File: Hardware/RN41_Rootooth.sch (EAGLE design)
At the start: 23 parts, among them Q1 MOSFET-NCHANNELSMD, Q2 MOSFET-NCHANNELSMD, U1 V_REG_317SMD, U2 BLUETOOTH-RN41, U3 V_REG_LDOSMD

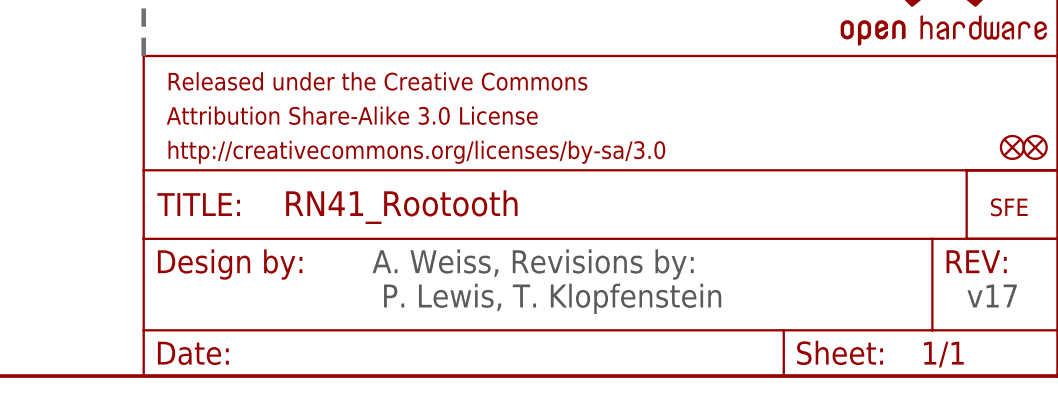
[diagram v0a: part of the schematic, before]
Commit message: Updated Revision to symbol layer
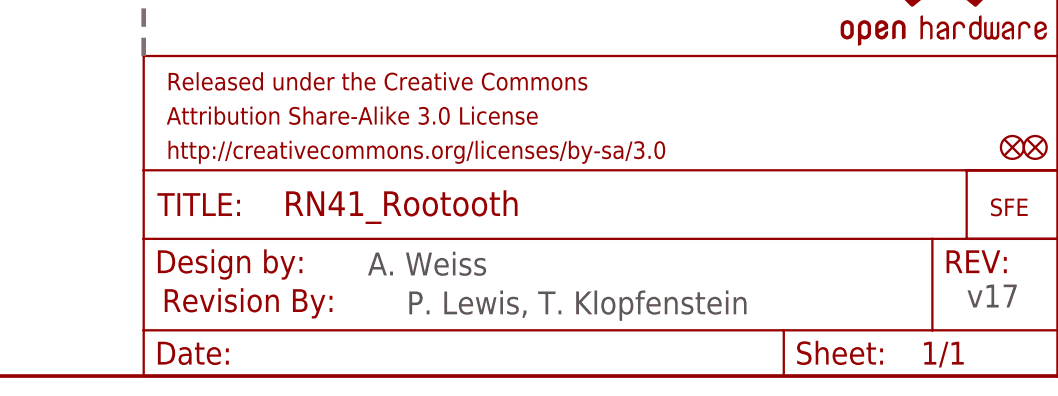
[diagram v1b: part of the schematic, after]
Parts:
- added U$2: REVISION, SparkFun-Aesthetics:REVISION
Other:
- note added: "A. Weiss"
- note added: "P. Lewis, T. Klopfenstein"
- note removed: "A. Weiss, Revisions by: P. Lewis, T. Klopfenstein"
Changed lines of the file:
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@@
 <grid distance="0.1" unitdist="inch" unit="inch" style="lines" multiple="1" display="no" altdistance="0.01" altunitdist="inch" altunit="inch"/>
 <layers>
-<layer number="1" name="Top" color="4" fill="1" visible="yes" active="no"/>
-<layer number="2" name="Route2" color="1" fill="3" visible="yes" active="no"/>
-<layer number="3" name="Route3" color="4" fill="3" visible="yes" active="no"/>
-<layer number="4" name="Route4" color="1" fill="4" visible="yes" active="no"/>
-<layer number="5" name="Route5" color="4" fill="4" visible="yes" active="no"/>
-<layer number="6" name="Route6" color="1" fill="8" visible="yes" active="no"/>
-<layer number="7" name="Route7" color="4" fill="8" visible="yes" active="no"/>
-<layer number="8" name="Route8" color="1" fill="2" visible="yes" active="no"/>
-<layer number="9" name="Route9" color="4" fill="2" visible="yes" active="no"/>
-<layer number="10" name="Route10" color="1" fill="7" visible="yes" active="no"/>
-<layer number="11" name="Route11" color="4" fill="7" visible="yes" active="no"/>
-<layer number="12" name="Route12" color="1" fill="5" visible="yes" active="no"/>
-<layer number="13" name="Route13" color="4" fill="5" visible="yes" active="no"/>
-<layer number="14" name="Route14" color="1" fill="6" visible="yes" active="no"/>
-<layer number="15" name="Route15" color="4" fill="6" visible="yes" active="no"/>
-<layer number="16" name="Bottom" color="1" fill="1" visible="yes" active="no"/>
-<layer number="17" name="Pads" color="2" fill="1" visible="yes" active="no"/>
-<layer number="18" name="Vias" color="2" fill="1" visible="yes" active="no"/>
-<layer number="19" name="Unrouted" color="6" fill="1" visible="yes" active="no"/>
-<layer number="20" name="Dimension" color="6" fill="1" visible="yes" active="no"/>
-<layer number="21" name="tPlace" color="16" fill="1" visible="yes" active="no"/>
-<layer number="22" name="bPlace" color="14" fill="1" visible="yes" active="no"/>
-<layer number="23" name="tOrigins" color="15" fill="1" visible="yes" active="no"/>
-<layer number="24" name="bOrigins" color="15" fill="1" visible="yes" active="no"/>
-<layer number="25" name="tNames" color="7" fill="1" visible="yes" active="no"/>
-<layer number="26" name="bNames" color="7" fill="1" visible="yes" active="no"/>
-<layer number="27" name="tValues" color="7" fill="1" visible="yes" active="no"/>
-<layer number="28" name="bValues" color="7" fill="1" visible="yes" active="no"/>
+<layer number="1" name="Top" color="4" fill="1" visible="no" active="no"/>
+<layer number="2" name="Route2" color="1" fill="3" visible="no" active="no"/>
+<layer number="3" name="Route3" color="4" fill="3" visible="no" active="no"/>
+<layer number="4" name="Route4" color="1" fill="4" visible="no" active="no"/>
+<layer number="5" name="Route5" color="4" fill="4" visible="no" active="no"/>
+<layer number="6" name="Route6" color="1" fill="8" visible="no" active="no"/>
+<layer number="7" name="Route7" color="4" fill="8" visible="no" active="no"/>
+<layer number="8" name="Route8" color="1" fill="2" visible="no" active="no"/>
+<layer number="9" name="Route9" color="4" fill="2" visible="no" active="no"/>
+<layer number="10" name="Route10" color="1" fill="7" visible="no" active="no"/>
+<layer number="11" name="Route11" color="4" fill="7" visible="no" active="no"/>
+<layer number="12" name="Route12" color="1" fill="5" visible="no" active="no"/>
+<layer number="13" name="Route13" color="4" fill="5" visible="no" active="no"/>
+<layer number="14" name="Route14" color="1" fill="6" visible="no" active="no"/>
+<layer number="15" name="Route15" color="4" fill="6" visible="no" active="no"/>
+<layer number="16" name="Bottom" color="1" fill="1" visible="no" active="no"/>
+<layer number="17" name="Pads" color="2" fill="1" visible="no" active="no"/>
+<layer number="18" name="Vias" color="2" fill="1" visible="no" active="no"/>
+<layer number="19" name="Unrouted" color="6" fill="1" visible="no" active="no"/>
+<layer number="20" name="Dimension" color="6" fill="1" visible="no" active="no"/>
+<layer number="21" name="tPlace" color="16" fill="1" visible="no" active="no"/>
+<layer number="22" name="bPlace" color="14" fill="1" visible="no" active="no"/>
+<layer number="23" name="tOrigins" color="15" fill="1" visible="no" active="no"/>
+<layer number="24" name="bOrigins" color="15" fill="1" visible="no" active="no"/>
+<layer number="25" name="tNames" color="7" fill="1" visible="no" active="no"/>
+<layer number="26" name="bNames" color="7" fill="1" visible="no" active="no"/>
+<layer number="27" name="tValues" color="7" fill="1" visible="no" active="no"/>
+<layer number="28" name="bValues" color="7" fill="1" visible="no" active="no"/>
 <layer number="29" name="tStop" color="7" fill="3" visible="no" active="no"/>
 <layer number="30" name="bStop" color="7" fill="6" visible="no" active="no"/>
@@
 <layer number="35" name="tGlue" color="7" fill="4" visible="no" active="no"/>
 <layer number="36" name="bGlue" color="7" fill="5" visible="no" active="no"/>
-<layer number="37" name="tTest" color="7" fill="1" visible="yes" active="no"/>
-<layer number="38" name="bTest" color="7" fill="1" visible="yes" active="no"/>
+<layer number="37" name="tTest" color="7" fill="1" visible="no" active="no"/>
+<layer number="38" name="bTest" color="7" fill="1" visible="no" active="no"/>
 <layer number="39" name="tKeepout" color="4" fill="11" visible="no" active="no"/>
 <layer number="40" name="bKeepout" color="1" fill="11" visible="no" active="no"/>
@@
 <layer number="44" name="Drills" color="7" fill="1" visible="no" active="no"/>
 <layer number="45" name="Holes" color="7" fill="1" visible="no" active="no"/>
-<layer number="46" name="Milling" color="3" fill="1" visible="yes" active="no"/>
-<layer number="47" name="Measures" color="7" fill="1" visible="yes" active="no"/>
-<layer number="48" name="Document" color="7" fill="1" visible="yes" active="no"/>
-<layer number="49" name="Reference" color="13" fill="1" visible="yes" active="no"/>
-<layer number="50" name="dxf" color="7" fill="1" visible="yes" active="no"/>
-<layer number="51" name="tDocu" color="6" fill="1" visible="yes" active="no"/>
-<layer number="52" name="bDocu" color="7" fill="1" visible="yes" active="no"/>
-<layer number="53" name="tGND_GNDA" color="7" fill="9" visible="yes" active="no"/>
-<layer number="54" name="bGND_GNDA" color="1" fill="9" visible="yes" active="no"/>
-<layer number="56" name="wert" color="7" fill="1" visible="yes" active="no"/>
+<layer number="46" name="Milling" color="3" fill="1" visible="no" active="no"/>
+<layer number="47" name="Measures" color="7" fill="1" visible="no" active="no"/>
+<layer number="48" name="Document" color="7" fill="1" visible="no" active="no"/>
+<layer number="49" name="Reference" color="13" fill="1" visible="no" active="no"/>
+<layer number="50" name="dxf" color="7" fill="1" visible="no" active="no"/>
+<layer number="51" name="tDocu" color="6" fill="1" visible="no" active="no"/>
+<layer number="52" name="bDocu" color="7" fill="1" visible="no" active="no"/>
+<layer number="53" name="tGND_GNDA" color="7" fill="9" visible="no" active="no"/>
+<layer number="54" name="bGND_GNDA" color="1" fill="9" visible="no" active="no"/>
+<layer number="56" name="wert" color="7" fill="1" visible="no" active="no"/>
 <layer number="91" name="Nets" color="2" fill="1" visible="yes" active="yes"/>
 <layer number="92" name="Busses" color="1" fill="1" visible="yes" active="yes"/>
@@
 <part name="JP3" library="SparkFun" deviceset="FIDUCIAL" device="UFIDUCIAL"/>
 <part name="LOGO1" library="SparkFun-Aesthetics" deviceset="OSHW-LOGO" device="S"/>
+<part name="U$2" library="SparkFun-Aesthetics" deviceset="REVISION" device=""/>
 </parts>
 <sheets>
@@
 <wire x1="0" y1="106.68" x2="147.32" y2="106.68" width="0.508" layer="95" style="shortdash"/>
 <text x="238.76" y="7.62" size="2.54" layer="97">v17</text>
-<text x="172.72" y="7.62" size="2.54" layer="97">A. Weiss, Revisions by:
- P. Lewis, T. Klopfenstein</text>
+<text x="172.212" y="11.176" size="2.54" layer="97">A. Weiss</text>
+<text x="176.53" y="6.858" size="2.54" layer="97">P. Lewis, T. Klopfenstein</text>
 </plain>
 <instances>
@@
 <instance part="JP3" gate="G$1" x="246.38" y="25.4"/>
 <instance part="LOGO1" gate="G$1" x="236.22" y="45.72"/>
+<instance part="U$2" gate="G$1" x="149.352" y="7.112"/>
 </instances>
 <busses>
@@
 </schematic>
 </drawing>
-<compatibility>
-<note version="6.3" minversion="6.2.2" severity="warning">
-Since Version 6.2.2 text objects can contain more than one line,
-which will not be processed correctly with this version.
-</note>
-</compatibility>
 </eagle>
